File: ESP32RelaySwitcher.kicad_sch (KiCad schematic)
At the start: 103 parts, among them J1 POWER_IN, J10 BUTTON_1, J11 BUTTON_2, J12 BUTTON_3, J13 BUTTON_4, J14 BUTTON_5, J15 BUTTON_6, J16 BUTTON_7, J17 BUTTON_8, J18 SERIAL+GPIO, J2 RELAY_1, J3 RELAY_2, J4 RELAY_4, J5 RELAY_3, J6 RELAY_5, J7 RELAY_6, J8 RELAY_8, J9 RELAY_7, K1 G6E-134P-US DC5, K2 G6E-134P-US DC5, K3 G6E-134P-US DC5, K4 G6E-134P-US DC5, K5 G6E-134P-US DC5, K6 G6E-134P-US DC5, K7 G6E-134P-US DC5, K8 G6E-134P-US DC5, Q1 2N7002, Q2 2N7002, Q3 2N7002, Q4 2N7002, Q5 2N7002, Q6 2N7002, Q7 2N7002, Q8 2N7002, SW1 POWER, SW2 RESET, SW3 IO0, U1 LMR36520ADDAR, U2 AP1117-33, U3 DHT22, U4 ESP32-WROOM-32D, U5 TSOP382xx

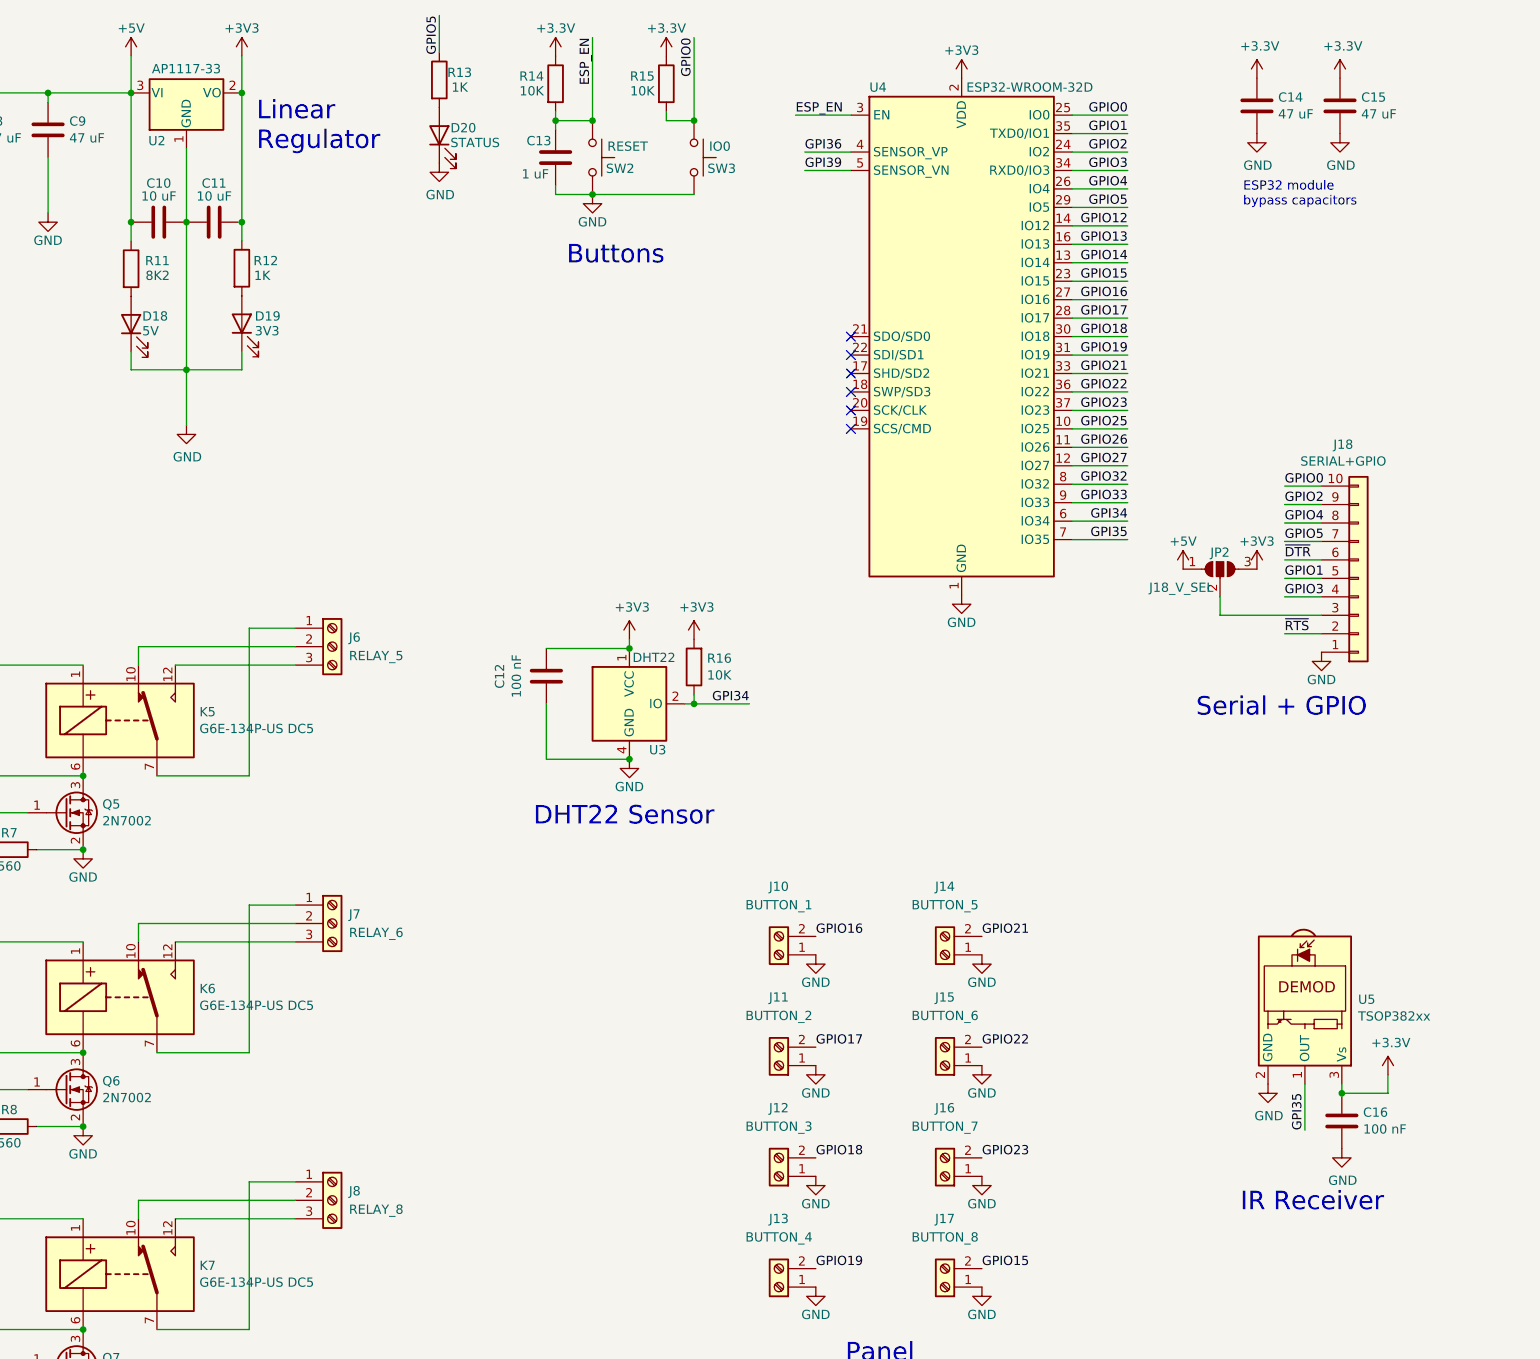
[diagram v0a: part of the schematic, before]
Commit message: Use parts I can actually get...
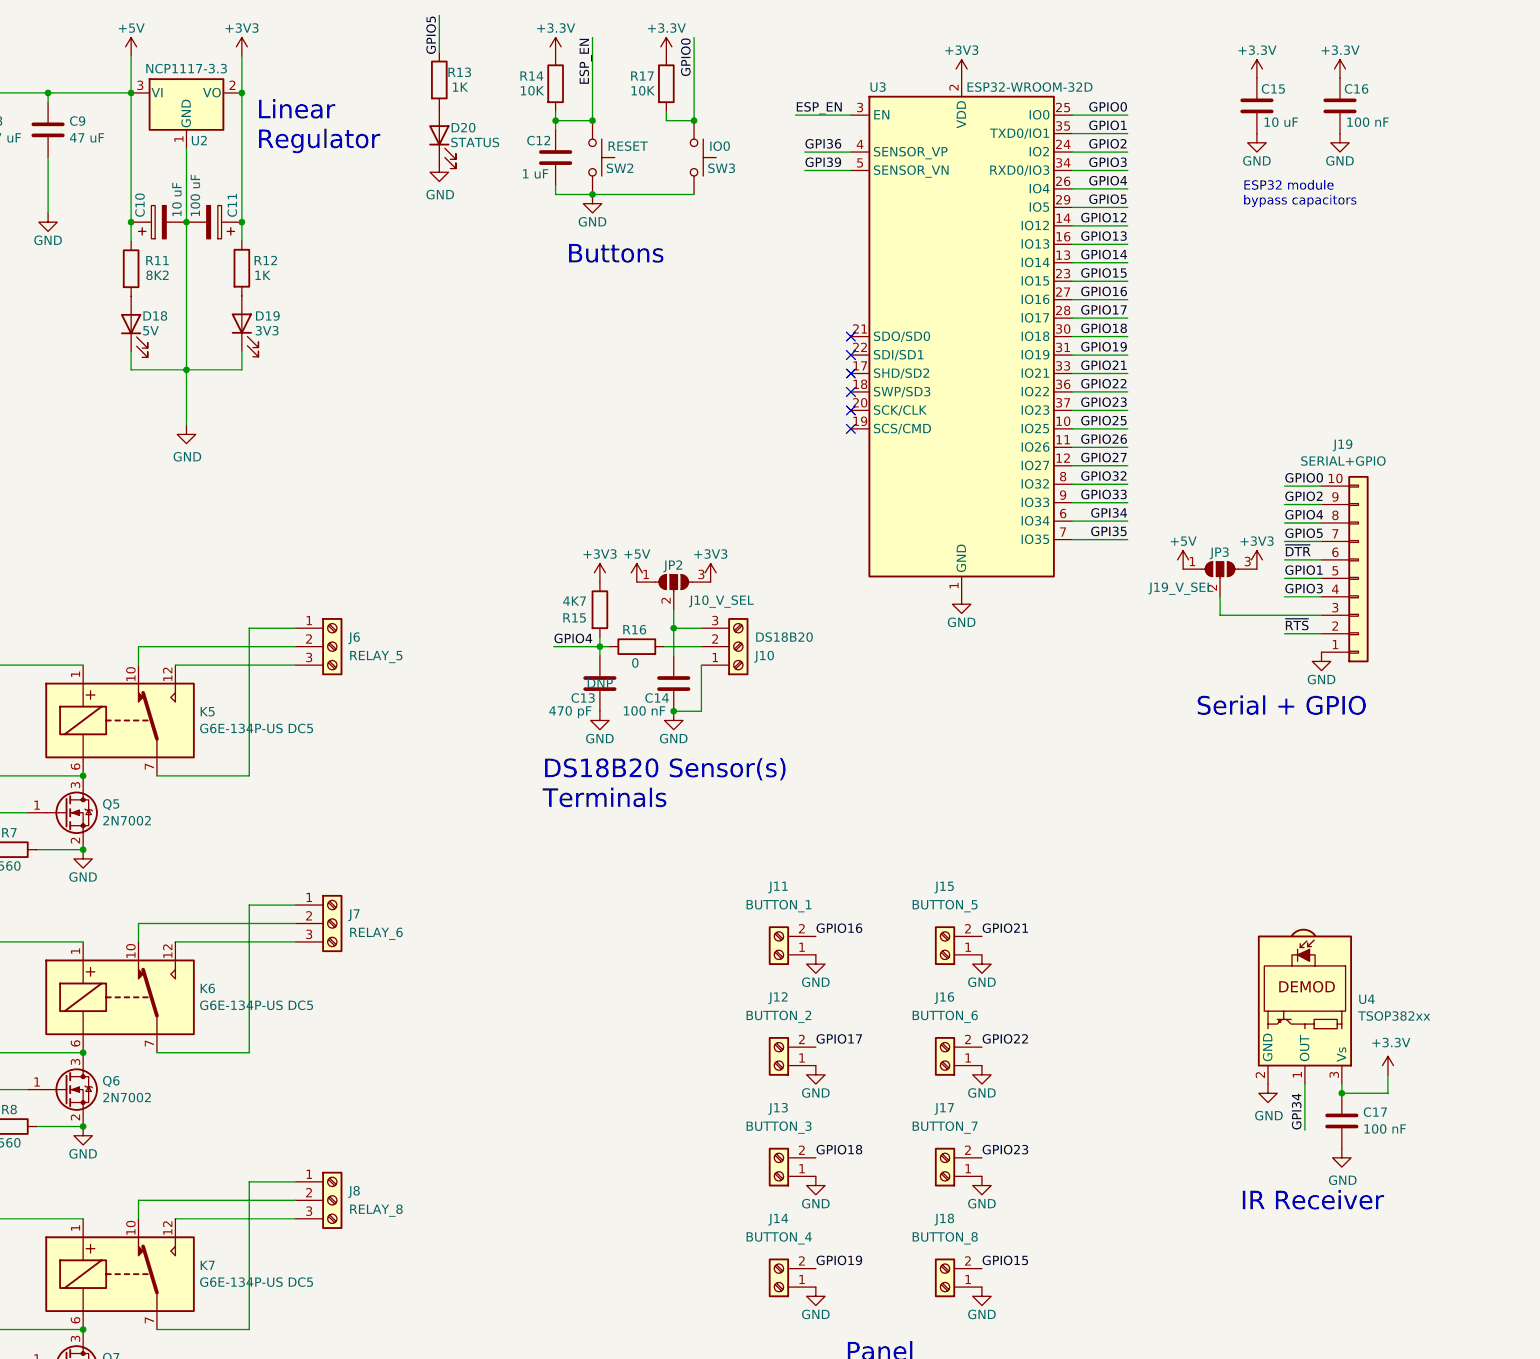
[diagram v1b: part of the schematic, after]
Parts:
- removed C10: 10 uF, Capacitor_SMD:C_0805_2012Metric, symbol Device:C
- removed C14, C15: 47 uF, Capacitor_SMD:C_0805_2012Metric, symbol Device:C
- removed U2: AP1117-33, Package_TO_SOT_SMD:SOT-223-3_TabPin2, symbol Regulator_Linear:AP1117-33
- removed U3: DHT22, Connector_PinSocket_2.54mm:PinSocket_1x04_P2.54mm_Vertical, symbol Sensor:DHT11
- added C10: 10 uF, Capacitor_SMD:CP_Elec_4x5.8, symbol Device:CP
- added C11: 100 uF, Capacitor_SMD:CP_Elec_5x5.4, symbol Device:CP
- added C13: 470 pF, Capacitor_SMD:C_0805_2012Metric, symbol Device:C
- added C16: 100 nF, Capacitor_SMD:C_0805_2012Metric, symbol Device:C
- added J10: DS18B20, TerminalBlock_Phoenix:TerminalBlock_Phoenix_PT-1,5-3-3.5-H_1x03_P3.50mm_Horizontal, symbol Connector:Screw_Terminal_01x03
- added JP2: J10_V_SEL, Jumper:SolderJumper-3_P1.3mm_Open_RoundedPad1.0x1.5mm, symbol Jumper:SolderJumper_3_Open
- added R16: 0, Resistor_SMD:R_0805_2012Metric, symbol Device:R
- added U2: NCP1117-3.3, Package_TO_SOT_SMD:TO-252-2, symbol Regulator_Linear:NCP1117-3.3_TO252
- JP3: renamed from JP2; value J18_V_SEL -> J19_V_SEL
- R15: renamed from R16; value 10K -> 4K7; Part RC0805FR-0710KL -> RC0805FR-074K7L
- renumbered C13 to C12, C12 to C14, C11 to C15, C16 to C17, J10 to J11, J11 to J12, J12 to J13, J13 to J14, J14 to J15, J15 to J16, J16 to J17, J17 to J18, J18 to J19, R15 to R17, U4 to U3, U5 to U4
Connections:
- net +3V3: now also C15.1, R15.1, C11.1, C16.1, JP2.3 (B), U2.2 (VO); no longer C14.1, C15.2, R15.2
- net +5V: now also C10.1, JP2.1 (A), U2.3 (VI)
- net GND: now also C15.2, C10.2, C11.2, C13.2, C16.2, J10.1 (Pin_1), U2.1 (GND); no longer C15.1
- net GPI34: now also U4.1 (OUT); no longer R15.1
- net GPI35: no longer U4.1 (OUT)
- net GPIO4: now also R15.2, C13.1, R16.1
- new net: J10.2 (Pin_2), R16.2
- new net: C14.1, J10.3 (Pin_3), JP2.2 (C)
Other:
- note added: "DS18B20 Sensor(s) Terminals"
- note removed: "DHT22 Sensor"
- moved on the sheet: C14, C15, R15

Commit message: Finishing
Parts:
- added J19: 3V3, Connector_PinSocket_2.54mm:PinSocket_1x02_P2.54mm_Vertical, symbol Connector_Generic:Conn_01x02
- added J20: 5V, Connector_PinSocket_2.54mm:PinSocket_1x02_P2.54mm_Vertical, symbol Connector_Generic:Conn_01x02
- JP3: value J19_V_SEL -> J21_V_SEL
- renumbered C17 to C16, C16 to C17, J19 to J21
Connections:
- net +3V3: now also J19.2 (Pin_2)
- net +5V: now also J20.2 (Pin_2)
- net GND: now also J19.1 (Pin_1), J20.1 (Pin_1)
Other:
- note added: "Aux. Power"
- moved on the sheet: C16, J21, JP3, U4

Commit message: Add BoM, update images
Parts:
- C10: MPN1 (none) -> AFK106M25B12T-F
- C11: MPN1 (none) -> UWR1A101MCL1GB
- C12: MPN1 C2012X5R1E105M125AA -> C0805C105K4RACTU
- C13: MPN1 (none) -> CC0805KRX7R9BB471
- C14, C16, C17: MPN1 (none) -> CC0805KRX7R7BB104
- J1, J11, J12, J13, J14, J15, J16, J17, J18: MPN1 (none) -> 1984617
- J10, J2, J3, J4, J5, J6, J7, J8, J9: MPN1 (none) -> 1984620
- R15: MPN1 (none) -> RC0805FR-074K7L
- R16: MPN1 (none) -> RC0805FR-070RL
- U2: MPN1 (none) -> LD1117DT33CTR
- U4: MPN1 (none) -> TSOP38238
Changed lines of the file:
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@@
       (effects (font (size 1.27 1.27)) hide)
     )
+    (property "MPN1" "LD1117DT33CTR" (id 4) (at 220.726 36.322 0)
+      (effects (font (size 1.27 1.27)) hide)
+    )
     (pin "1")
     (pin "2")
@@
       (effects (font (size 1.27 1.27)) hide)
     )
+    (property "MPN1" "1984617" (id 4) (at 31.496 38.862 0)
+      (effects (font (size 1.27 1.27)) hide)
+    )
     (pin "1")
     (pin "2")
@@
       (effects (font (size 1.27 1.27)) hide)
     )
+    (property "MPN1" "RC0805FR-070RL" (id 5) (at 282.702 112.522 0)
+      (effects (font (size 1.27 1.27)) hide)
+    )
     (pin "1")
     (pin "2")
@@
       (effects (font (size 1.27 1.27)) hide)
     )
+    (property "MPN1" "1984620" (id 4) (at 154.432 188.722 0)
+      (effects (font (size 1.27 1.27)) hide)
+    )
     (pin "1")
     (pin "2")
@@
       (effects (font (size 1.27 1.27)) hide)
     )
+    (property "MPN1" "1984617" (id 4) (at 325.12 154.94 0)
+      (effects (font (size 1.27 1.27)) hide)
+    )
     (pin "1")
     (pin "2")
@@
       (effects (font (size 1.27 1.27)) hide)
     )
-    (property "MPN1" "C2012X5R1E105M125AA" (id 5) (at 271.526 45.212 0)
+    (property "MPN1" "C0805C105K4RACTU" (id 5) (at 271.526 45.212 0)
       (effects (font (size 1.27 1.27)) hide)
     )
@@
       (effects (font (size 1.27 1.27)) hide)
     )
+    (property "MPN1" "1984617" (id 4) (at 325.12 185.42 0)
+      (effects (font (size 1.27 1.27)) hide)
+    )
     (pin "1")
     (pin "2")
@@
       (effects (font (size 1.27 1.27)) hide)
     )
+    (property "MPN1" "1984620" (id 4) (at 154.432 226.822 0)
+      (effects (font (size 1.27 1.27)) hide)
+    )
     (pin "1")
     (pin "2")
@@
       (effects (font (size 1.27 1.27)) hide)
     )
+    (property "MPN1" "TSOP38238" (id 4) (at 374.142 124.968 0)
+      (effects (font (size 1.27 1.27)) hide)
+    )
     (pin "1")
     (pin "2")
@@
       (effects (font (size 1.27 1.27)) hide)
     )
+    (property "MPN1" "1984620" (id 4) (at 240.792 188.722 0)
+      (effects (font (size 1.27 1.27)) hide)
+    )
     (pin "1")
     (pin "2")
@@
       (effects (font (size 1.27 1.27)) hide)
     )
+    (property "MPN1" "1984620" (id 4) (at 240.792 150.622 0)
+      (effects (font (size 1.27 1.27)) hide)
+    )
     (pin "1")
     (pin "2")
@@
       (effects (font (size 1.27 1.27)) hide)
     )
+    (property "MPN1" "1984617" (id 4) (at 325.12 170.18 0)
+      (effects (font (size 1.27 1.27)) hide)
+    )
     (pin "1")
     (pin "2")
@@
       (effects (font (size 1.524 1.524)) hide)
     )
+    (property "MPN1" "UWR1A101MCL1GB" (id 5) (at 224.536 54.102 0)
+      (effects (font (size 1.27 1.27)) hide)
+    )
     (pin "1")
     (pin "2")
@@
       (effects (font (size 1.27 1.27)) hide)
     )
+    (property "MPN1" "1984617" (id 4) (at 302.26 170.18 0)
+      (effects (font (size 1.27 1.27)) hide)
+    )
     (pin "1")
     (pin "2")
@@
       (effects (font (size 1.27 1.27)) hide)
     )
+    (property "MPN1" "CC0805KRX7R7BB104" (id 5) (at 379.476 38.1 0)
+      (effects (font (size 1.27 1.27)) hide)
+    )
     (pin "1")
     (pin "2")
@@
       (effects (font (size 1.27 1.27)) hide)
     )
+    (property "MPN1" "1984617" (id 4) (at 302.26 154.94 0)
+      (effects (font (size 1.27 1.27)) hide)
+    )
     (pin "1")
     (pin "2")
@@
     )
     (property "Population" "DNP" (id 5) (at 277.622 117.602 0))
+    (property "MPN1" "CC0805KRX7R9BB471" (id 6) (at 277.622 117.602 0)
+      (effects (font (size 1.27 1.27)) hide)
+    )
     (pin "1")
     (pin "2")
@@
       (effects (font (size 1.27 1.27)) hide)
     )
+    (property "MPN1" "RC0805FR-074K7L" (id 5) (at 277.622 107.442 0)
+      (effects (font (size 1.27 1.27)) hide)
+    )
     (pin "1")
     (pin "2")
@@
       (effects (font (size 1.27 1.27)) hide)
     )
+    (property "MPN1" "CC0805KRX7R7BB104" (id 5) (at 379.222 140.208 0)
+      (effects (font (size 1.27 1.27)) hide)
+    )
     (pin "1")
     (pin "2")
@@
       (effects (font (size 1.27 1.27)) hide)
     )
+    (property "MPN1" "1984620" (id 4) (at 240.792 112.522 0)
+      (effects (font (size 1.27 1.27)) hide)
+    )
     (pin "1")
     (pin "2")
@@
       (effects (font (size 1.27 1.27)) hide)
     )
+    (property "MPN1" "1984620" (id 4) (at 296.672 112.522 0)
+      (effects (font (size 1.27 1.27)) hide)
+    )
     (pin "1")
     (pin "2")
@@
       (effects (font (size 1.27 1.27)) hide)
     )
+    (property "MPN1" "1984617" (id 4) (at 302.26 200.66 0)
+      (effects (font (size 1.27 1.27)) hide)
+    )
     (pin "1")
     (pin "2")
@@
       (effects (font (size 1.27 1.27)) hide)
     )
+    (property "MPN1" "1984617" (id 4) (at 302.26 185.42 0)
+      (effects (font (size 1.27 1.27)) hide)
+    )
     (pin "1")
     (pin "2")
@@
       (effects (font (size 1.27 1.27)) hide)
     )
+    (property "MPN1" "1984620" (id 4) (at 154.432 150.622 0)
+      (effects (font (size 1.27 1.27)) hide)
+    )
     (pin "1")
     (pin "2")
@@
       (effects (font (size 1.27 1.27)) hide)
     )
+    (property "MPN1" "CC0805KRX7R7BB104" (id 5) (at 287.782 117.602 0)
+      (effects (font (size 1.27 1.27)) hide)
+    )
     (pin "1")
     (pin "2")
@@
       (effects (font (size 1.524 1.524)) hide)
     )
+    (property "MPN1" "AFK106M25B12T-F" (id 5) (at 216.916 54.102 0)
+      (effects (font (size 1.27 1.27)) hide)
+    )
     (pin "1")
     (pin "2")
@@
       (effects (font (size 1.27 1.27)) hide)
     )
+    (property "MPN1" "1984617" (id 4) (at 325.12 200.66 0)
+      (effects (font (size 1.27 1.27)) hide)
+    )
     (pin "1")
     (pin "2")
@@
       (effects (font (size 1.27 1.27)) hide)
     )
+    (property "MPN1" "1984620" (id 4) (at 154.432 112.522 0)
+      (effects (font (size 1.27 1.27)) hide)
+    )
     (pin "1")
     (pin "2")
@@
       (effects (font (size 1.27 1.27)) hide)
     )
+    (property "MPN1" "1984620" (id 4) (at 240.792 226.822 0)
+      (effects (font (size 1.27 1.27)) hide)
+    )
